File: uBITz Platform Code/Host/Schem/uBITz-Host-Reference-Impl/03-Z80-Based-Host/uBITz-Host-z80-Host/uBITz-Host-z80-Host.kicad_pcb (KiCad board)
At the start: 4 copper layers, 84.3 x 100 mm, 60 parts, among them J2 12401610E4_2A, J3 Conn_01x02_Pin, J4 Conn_02x05_Top_Bottom, U1 SN74LS612N, U10 SN74LVC245ADGVR, U11 24LC16BT-I_SN, U12 SN74LVC245ADGVR, U13 SN74LVC245ADGVR, U2 Z084000xP, U3 FT232HL, U4 93LC56BT-I/OT, U5 ATF1504AS-10AU100, U6 SN74LVC245ADGVR, U7 MAX662ACSA_T, U8 SN74LVC245ADGVR, U9 SN74LVC245ADGVR, Y1 ACH-14.31818MHZ-EK, Y2 ECS-2033-120-BN

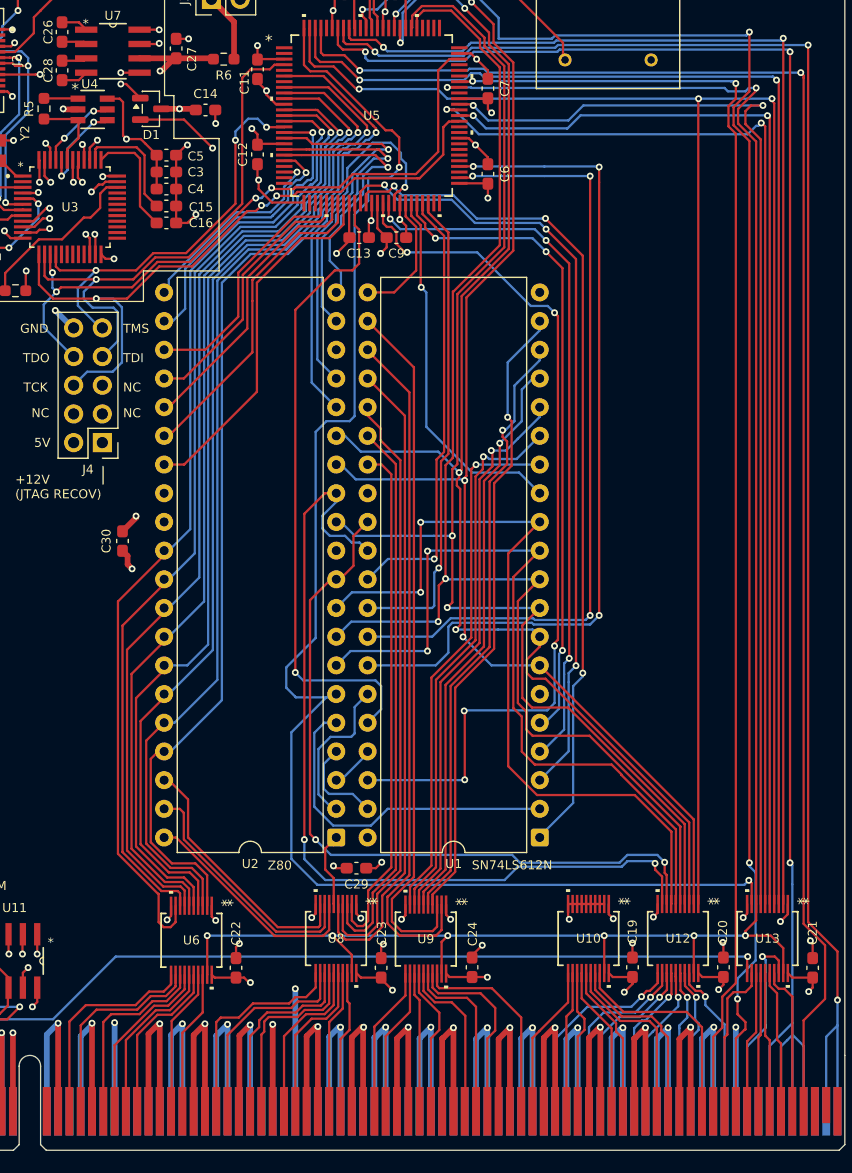
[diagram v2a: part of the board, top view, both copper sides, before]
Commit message: Added the ability to tri-state the MEM0_CS and MEM1_CS signals to allow the Dock to take over memory type selection based on addresses
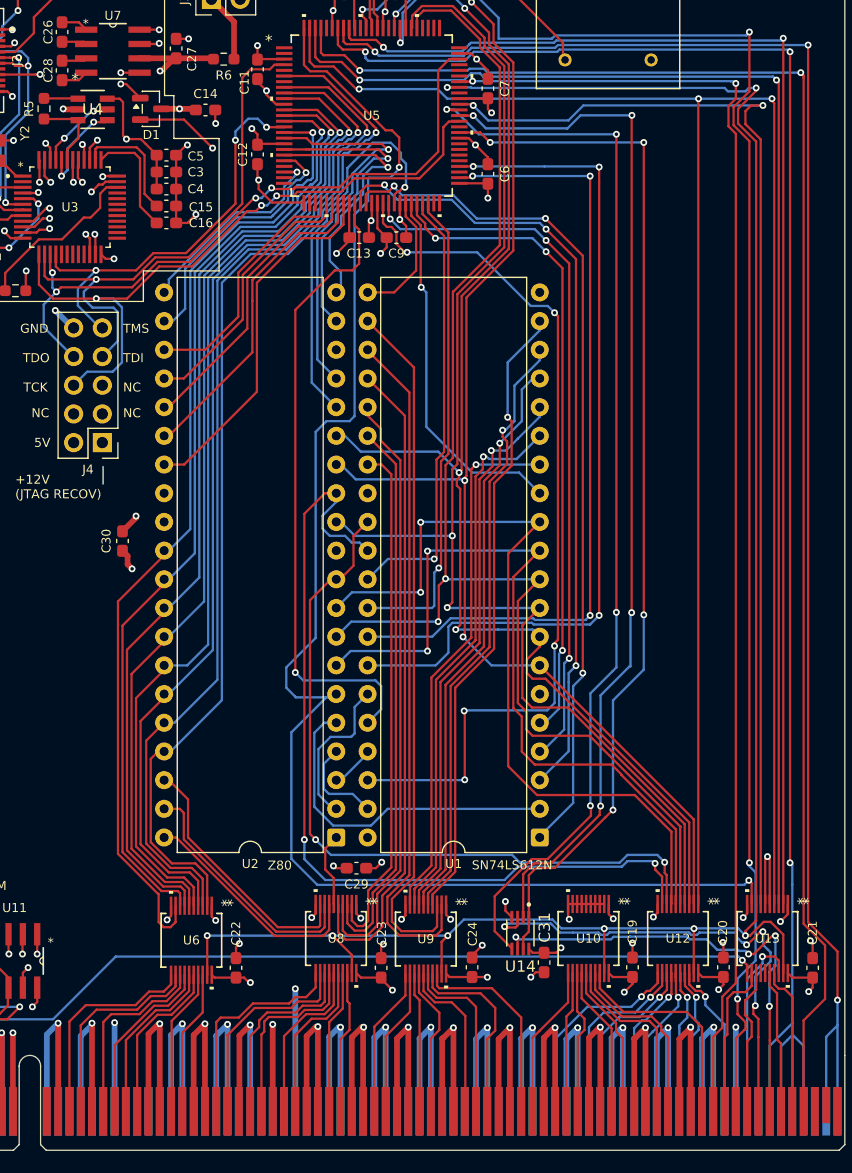
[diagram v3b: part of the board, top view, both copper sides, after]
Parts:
- added C31: 100n, Capacitor_SMD:C_0603_1608Metric_Pad1.08x0.95mm_HandSolder, F.Cu at (147.7, 141.8)
- added U14: SN74LVC2G126DCUR, Footprints:SOP50P310X90-8N, F.Cu at (145.6, 139.2)
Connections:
- U13 pad 14: /~{B_MEM0_CS} -> unconnected-(U13-B5-Pad14)
- U13 pad 15: /~{B_MEM1_CS} -> unconnected-(U13-B4-Pad15)
- U13 pad 5: /~{BUS_MEM1_CS} -> GND
- U13 pad 6: /~{BUS_MEM0_CS} -> GND
- U5 pad 60: unconnected-(U5-I/O-Pad60) -> /~{BUS_MEM_CS_Z}
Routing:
- net /~{BUS_MEM_CS_Z}: track 0.00 -> 93.5 mm, vias 0 -> 4
- net /~{B_MEM0_CS}: track 12.3 -> 43.8 mm, vias 0 -> 4
- net /~{B_MEM1_CS}: track 12.4 -> 41.4 mm, vias 0 -> 4
- net GND: track 604.1 -> 616.0 mm, vias 96 -> 99
- net /~{BUS_MEM1_CS}: track 98.4 -> 92.2 mm, vias 2 -> 4
- net /~{BUS_MEM0_CS}: track 99.6 -> 95.2 mm, vias 2 -> 4
- net /~{BUS_DMA_GNT}: track 176.7 -> 180.9 mm
- net +3V3: track 58.1 -> 61.3 mm, vias 13 -> 14
- net /~{B_MREQ}: track 12.6 -> 13.1 mm
- net /B_CLK_HOST: track 79.6 -> 79.1 mm

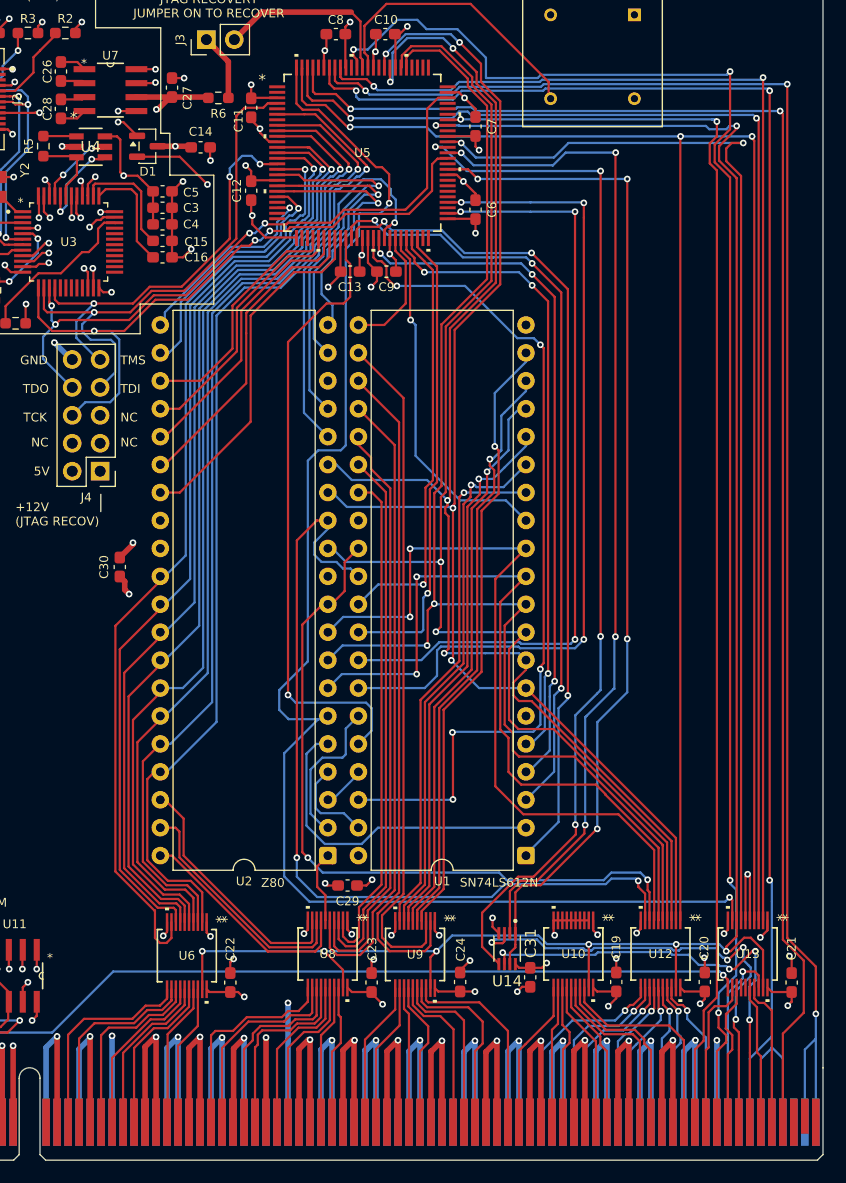
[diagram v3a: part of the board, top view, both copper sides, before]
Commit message: Modified Pinout for easier layout Moved processing of MEM0_CS and MEM1_CS to Dock, no longer needed on Host
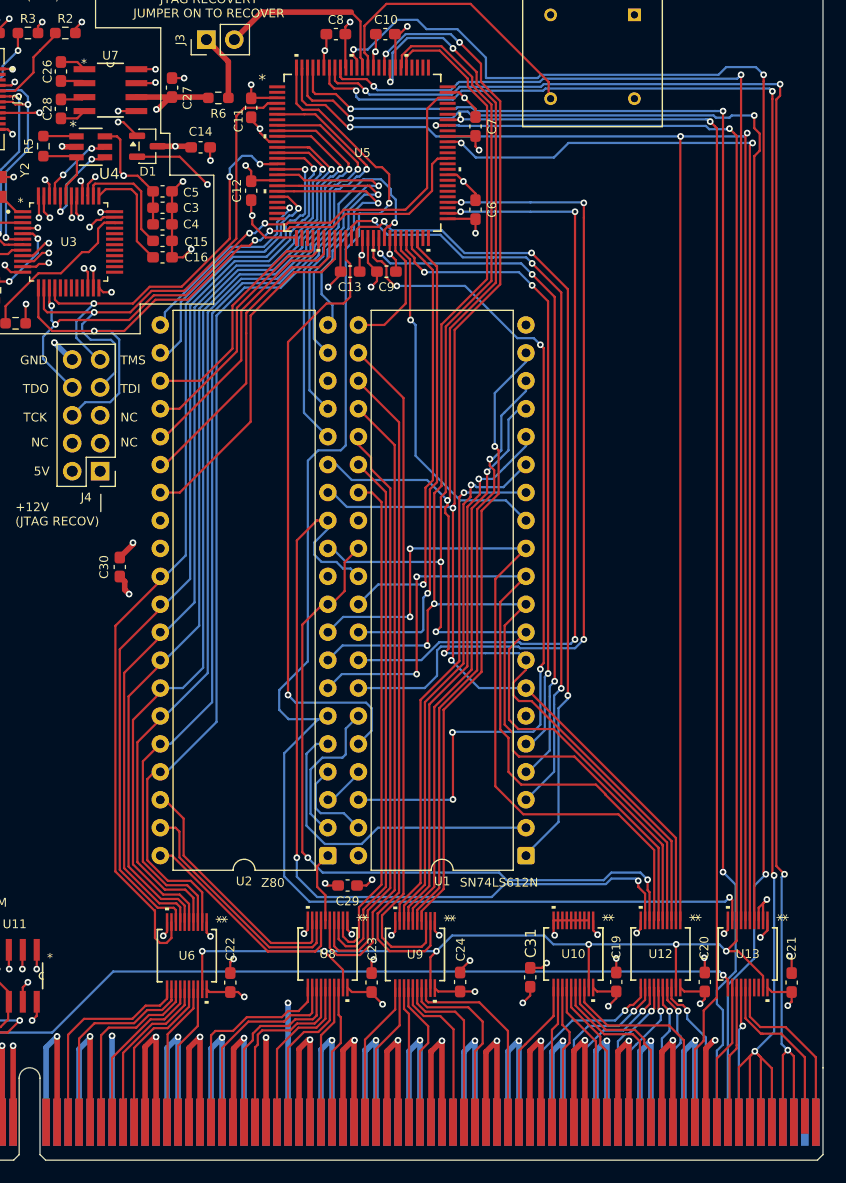
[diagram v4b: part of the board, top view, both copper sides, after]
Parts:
- removed U14: SN74LVC2G126DCUR, Footprints:SOP50P310X90-8N
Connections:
- J1 pad A73: GND -> /~{BUS_READY}
- J1 pad A74: /~{B_CPU_ACK} -> /~{BUS_RESET}
- J1 pad A75: unconnected-(J1A-~{INT_ACK}-PadA75) -> /B_R/~{W}
- J1 pad A76: /~{BUS_CPU_INT} -> unconnected-(J1A-~{MEM0_CS}-PadA76)
- J1 pad A77: /~{BUS_CPU_INT} -> unconnected-(J1A-~{MEM1_CS}-PadA77)
- J1 pad A78: /~{BUS_CPU_INT} -> unconnected-(J1A-~{CS}-PadA78)
- J1 pad A79: /~{BUS_CPU_INT} -> unconnected-(J1A-~{INT_ACK}-PadA79)
- J1 pad A81: /~{BUS_CPU_NMI} -> unconnected-(J1A-~{INT_CH0}-PadA81)
- J1 pad A82: /~{BUS_CPU_NMI} -> unconnected-(J1A-~{INT_CH1}-PadA82)
- J1 pad B72: /~{B_DMA_GNT} -> GND
- J1 pad B73: /~{BUS_RESET} -> /~{B_DMA_GNT}
- J1 pad B74: /~{B_MREQ} -> /~{B_CPU_ACK}
- J1 pad B75: /~{B_MEM0_CS} -> /~{BUS_CPU_INT}
- J1 pad B76: /~{B_MEM1_CS} -> /~{BUS_CPU_INT}
- J1 pad B77: /B_R/~{W} -> /~{BUS_CPU_INT}
- J1 pad B78: /~{B_IORQ} -> /~{BUS_CPU_INT}
- J1 pad B79: /~{BUS_READY} -> /~{BUS_CPU_NMI}
- J1 pad B80: unconnected-(J1A-~{CS}-PadB80) -> /~{BUS_CPU_NMI}
- J1 pad B81: unconnected-(J1A-~{INT_CH0}-PadB81) -> /~{B_MREQ}
- J1 pad B82: unconnected-(J1A-~{INT_CH1}-PadB82) -> /~{B_IORQ}
- U13 pad 13: /~{B_MREQ} -> /~{B_CPU_ACK}
- U13 pad 14: unconnected-(U13-B5-Pad14) -> /B_R/~{W}
- U13 pad 15: unconnected-(U13-B4-Pad15) -> /~{B_MREQ}
- U13 pad 16: /B_R/~{W} -> /~{B_IORQ}
- U13 pad 17: /~{B_IORQ} -> unconnected-(U13-B2-Pad17)
- U13 pad 18: /~{B_CPU_ACK} -> unconnected-(U13-B1-Pad18)
- U13 pad 2: /~{BUS_CPU_ACK} -> GND
- U13 pad 3: /~{BUS_IORQ} -> GND
- U13 pad 4: /BUS_R/~{W} -> /~{BUS_IORQ}
- U13 pad 5: GND -> /~{BUS_MREQ}
- U13 pad 6: GND -> /BUS_R/~{W}
- U13 pad 7: /~{BUS_MREQ} -> /~{BUS_CPU_ACK}
- U5 pad 60: /~{BUS_MEM_CS_Z} -> unconnected-(U5-I/O-Pad60)
- U5 pad 63: /~{BUS_MEM1_CS} -> unconnected-(U5-I/O-Pad63)
- U5 pad 64: /~{BUS_MEM0_CS} -> unconnected-(U5-I/O-Pad64)
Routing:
- net /~{BUS_MEM0_CS}: track 95.2 -> 0.00 mm, vias 4 -> 0
- net /~{BUS_MEM_CS_Z}: track 93.5 -> 0.00 mm, vias 4 -> 0
- net /~{BUS_MEM1_CS}: track 92.2 -> 0.00 mm, vias 4 -> 0
- net /~{B_MEM0_CS}: track 43.8 -> 0.00 mm, vias 4 -> 0
- net /~{B_MEM1_CS}: track 41.4 -> 0.00 mm, vias 4 -> 0
- net GND: track 616.0 -> 610.5 mm, vias 99 -> 98
- net /~{BUS_READY}: track 139.3 -> 133.9 mm, vias 2 -> 3
- net /~{BUS_DMA_GNT}: track 180.9 -> 176.4 mm
- net /~{B_CPU_ACK}: track 17.0 -> 12.6 mm, vias 1 -> 0
- net /~{B_IORQ}: track 13.2 -> 16.1 mm
- net /~{BUS_CPU_NMI}: track 146.7 -> 144.7 mm, vias 3 -> 4
- net /~{BUS_RESET}: track 139.0 -> 140.9 mm, vias 4 -> 3
- net /~{B_MREQ}: track 13.1 -> 15.0 mm
- net /~{BUS_CPU_ACK}: track 117.1 -> 115.2 mm
- net +3V3: track 61.3 -> 59.8 mm
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
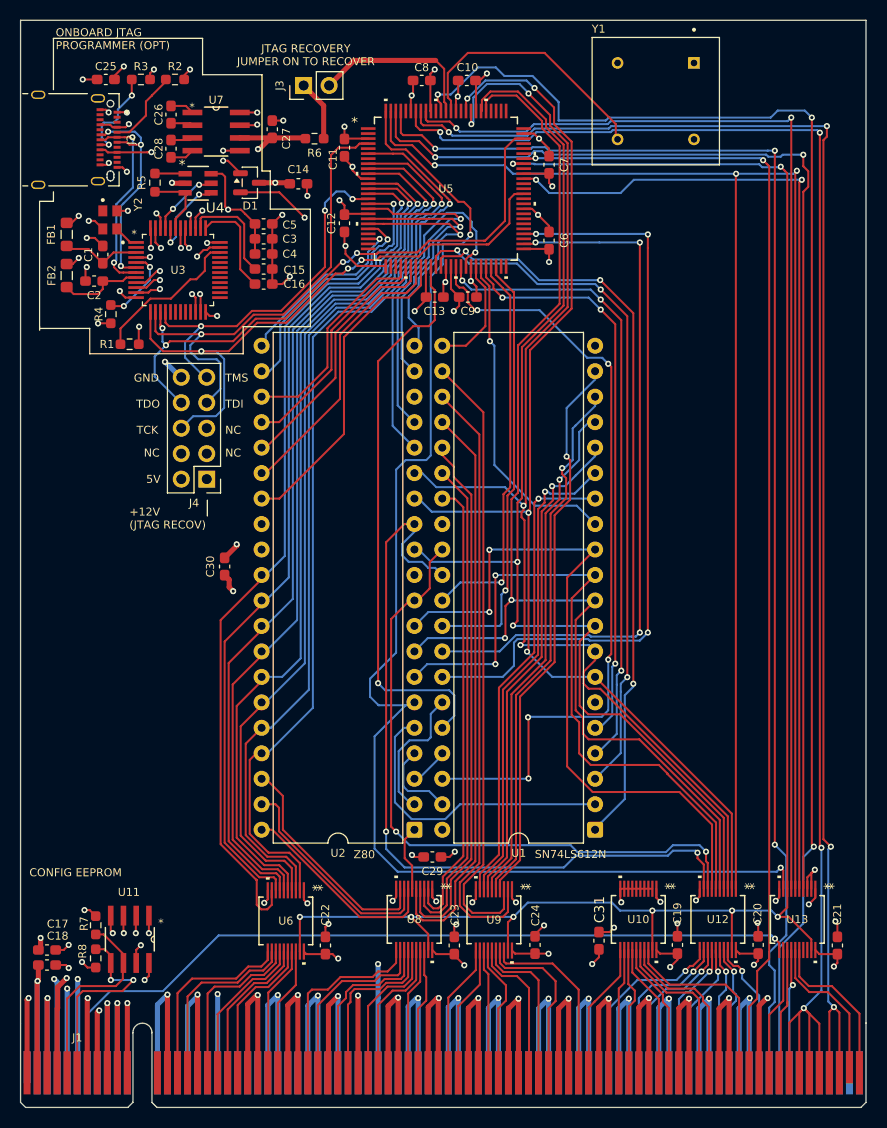
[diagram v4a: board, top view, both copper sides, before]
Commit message: Removed transceivers from Z80 host with the mapper and cleaned up schematics
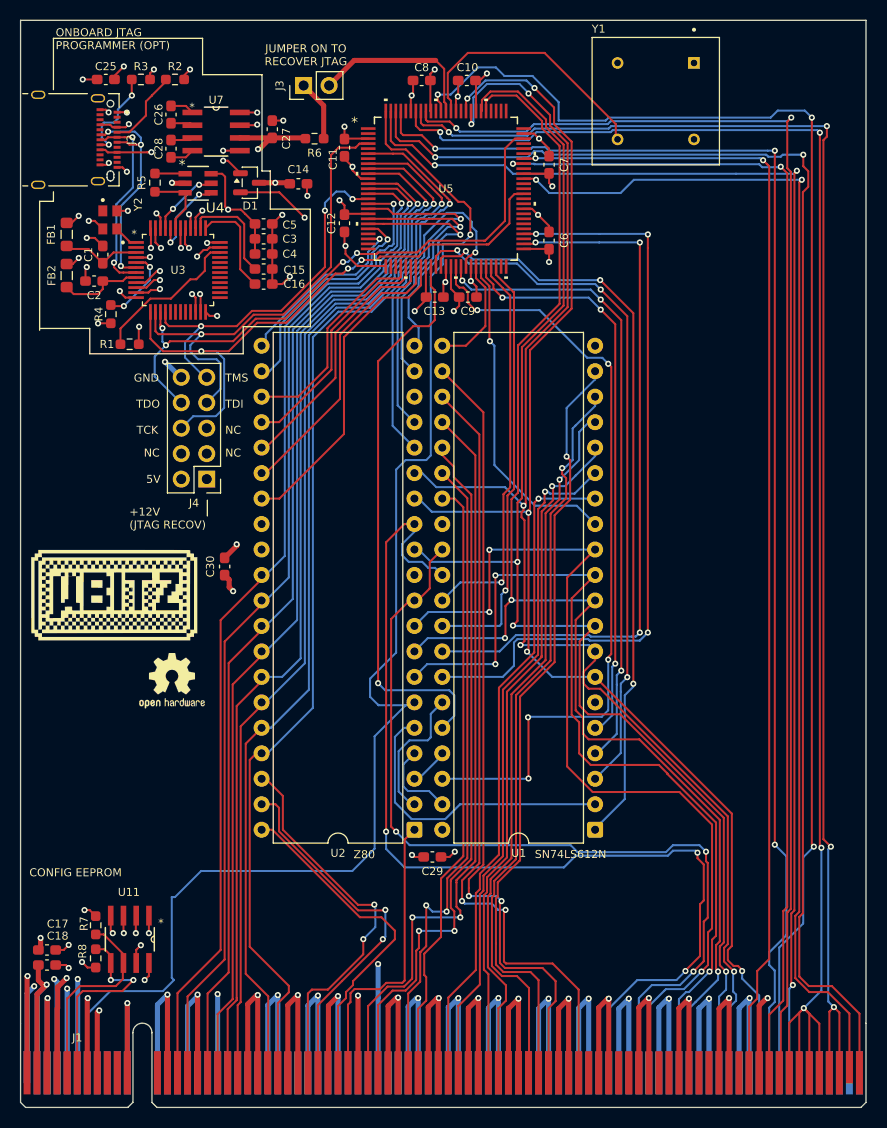
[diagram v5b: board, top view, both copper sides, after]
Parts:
- removed C19, C20, C21, C22, C23, C24, C31: 100n, Capacitor_SMD:C_0603_1608Metric_Pad1.08x0.95mm_HandSolder
- removed U10, U12, U13, U6, U8, U9: SN74LVC245ADGVR, Footprints:DGV20-M
- added G***: LOGO, Footprints:uBITz Logo, F.Cu at (99.4, 107.5)
- added REF**: OSHW-Logo2_7.3x6mm_SilkScreen, Symbol:OSHW-Logo2_7.3x6mm_SilkScreen, F.Cu at (105.2, 115.9)
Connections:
- J1 pad A1: unconnected-(J1C-~{DRV5V}-PadA1) -> GND
- J1 pad A10: +3V3 -> unconnected-(J1C-+3V3_MAIN-PadA10)
- J1 pad A11: unconnected-(J1C-~{SENS3V}-PadA11) -> GND
- J1 pad A57: /B_D7 -> /D7
- J1 pad A60: /B_D6 -> /D6
- J1 pad A61: /B_D5 -> /D5
- J1 pad A64: /B_D4 -> /D4
- J1 pad A65: /B_D3 -> /D3
- J1 pad A68: /B_D2 -> /D2
- J1 pad A69: /B_D1 -> /D1
- J1 pad A7: /B_CLK_HOST -> /CPUCLK
- J1 pad A72: /B_D0 -> /D0
- J1 pad A75: /B_R/~{W} -> /BUS_R/~{W}
- J1 pad A9: +3V3 -> unconnected-(J1C-+3V3_MAIN-PadA9)
- J1 pad B10: +3V3 -> unconnected-(J1C-+3V3_MAIN-PadB10)
- J1 pad B14: /B_A0 -> /A0
- J1 pad B15: /B_A1 -> /A1
- J1 pad B17: /B_A2 -> /A2
- J1 pad B18: /B_A3 -> /A3
- J1 pad B19: /B_A4 -> /A4
- J1 pad B20: /B_A5 -> /A5
- J1 pad B23: /B_A6 -> /A6
- J1 pad B24: /B_A7 -> /A7
- J1 pad B27: /B_A8 -> /A8
- J1 pad B28: /B_A9 -> /A9
- J1 pad B30: /B_A10 -> /A10
- J1 pad B31: /B_A11 -> /A11
- J1 pad B33: /B_A12 -> /A12
- J1 pad B34: /B_A13 -> /A13
- J1 pad B37: /B_A14 -> /A14
- J1 pad B38: /B_A15 -> /A15
- J1 pad B41: /B_A16 -> /A16
- J1 pad B42: /B_A17 -> /A17
- J1 pad B45: /B_A18 -> /A18
- J1 pad B46: /B_A19 -> /A19
- J1 pad B49: /B_A20 -> /A20
- J1 pad B50: /B_A21 -> /A21
- J1 pad B51: /B_A22 -> /A22
- J1 pad B54: /B_A23 -> /A23
- J1 pad B55: /B_A24 -> unconnected-(J1A-A24-PadB55)
- J1 pad B58: /B_A25 -> unconnected-(J1A-A25-PadB58)
- J1 pad B59: /B_A26 -> unconnected-(J1A-A26-PadB59)
- J1 pad B62: /B_A27 -> unconnected-(J1A-A27-PadB62)
- J1 pad B63: /B_A28 -> unconnected-(J1A-A28-PadB63)
- J1 pad B66: /B_A29 -> unconnected-(J1A-A29-PadB66)
- J1 pad B67: /B_A30 -> unconnected-(J1A-A30-PadB67)
- J1 pad B70: /B_A31 -> unconnected-(J1A-A31-PadB70)
- J1 pad B73: /~{B_DMA_GNT} -> /~{BUS_DMA_GNT}
- J1 pad B74: /~{B_CPU_ACK} -> /~{BUS_CPU_ACK}
- J1 pad B81: /~{B_MREQ} -> /~{BUS_MREQ}
- J1 pad B82: /~{B_IORQ} -> /~{BUS_IORQ}
- J1 pad B9: +3V3 -> unconnected-(J1C-+3V3_MAIN-PadB9)
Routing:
- net /B_CLK_HOST: track 79.1 -> 0.00 mm, vias 1 -> 0
- net +3V3: track 59.8 -> 0.00 mm, vias 14 -> 0
- net /~{BUS_DMA_GNT}: track 176.4 -> 119.2 mm, vias 8 -> 2
- net /BUS_R/~{W}: track 188.0 -> 135.4 mm
- net /D7: track 79.5 -> 104.0 mm, vias 2 -> 3
- net /D6: track 67.1 -> 89.9 mm, vias 2 -> 3
- net /A11: track 8.28 -> 31.0 mm
- net /~{BUS_IORQ}: track 118.2 -> 140.5 mm
- net /D5: track 71.1 -> 93.1 mm, vias 2 -> 3
- net /A21: track 55.9 -> 77.7 mm
- net /~{BUS_MREQ}: track 99.7 -> 121.0 mm
- net /A20: track 53.7 -> 74.6 mm
- net /D0: track 115.3 -> 135.3 mm, vias 4 -> 5
- net /D4: track 69.6 -> 89.6 mm, vias 2 -> 3
- net /D3: track 119.1 -> 138.9 mm, vias 2 -> 3
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- removed copper zone on In2.Cu, net +3V3
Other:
- board text added: "JUMPER ON TO RECOVER JTAG"
- board text removed: "JTAG RECOVERY JUMPER ON TO RECOVER"
